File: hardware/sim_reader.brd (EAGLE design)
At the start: 29.2 x 20.3 mm, 15 parts, among them IC1 74AC04D, X1 3.57 MHz

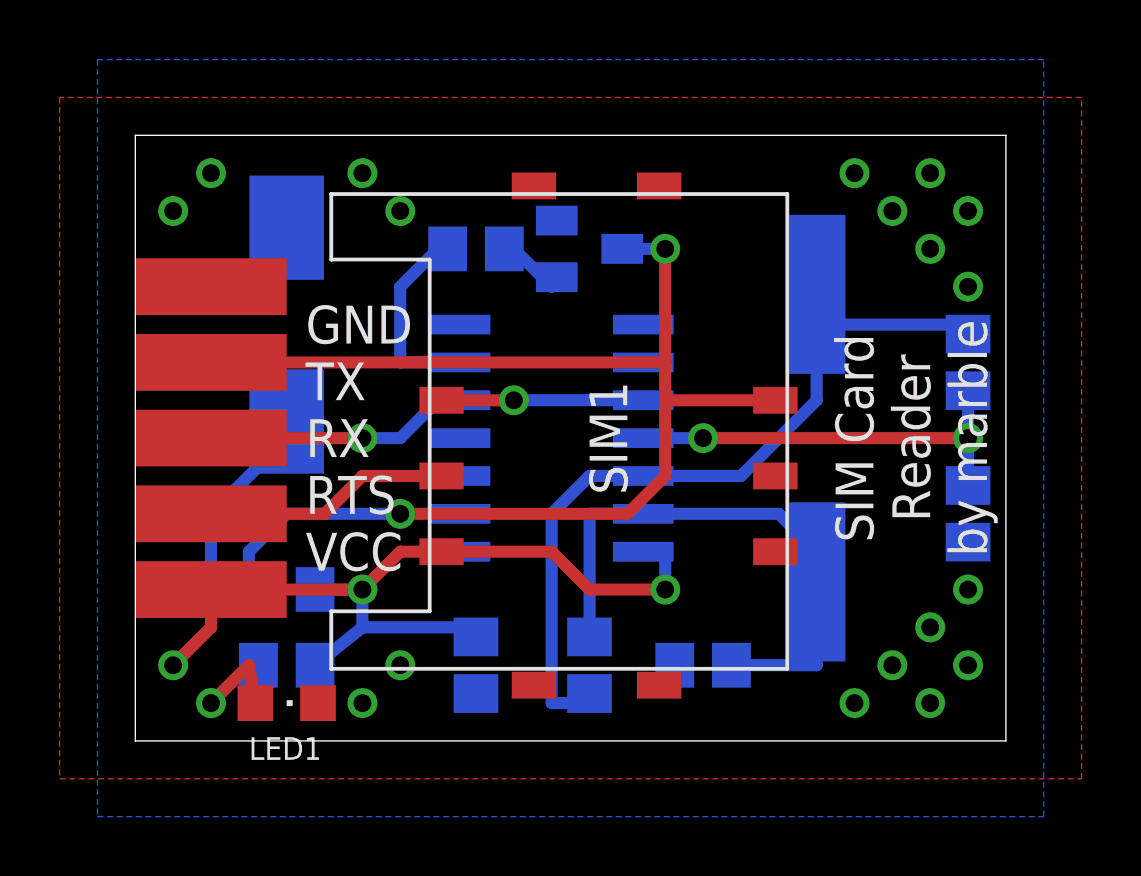
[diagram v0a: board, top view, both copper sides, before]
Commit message: redisgned. now compatible to most USB UART converters; very small
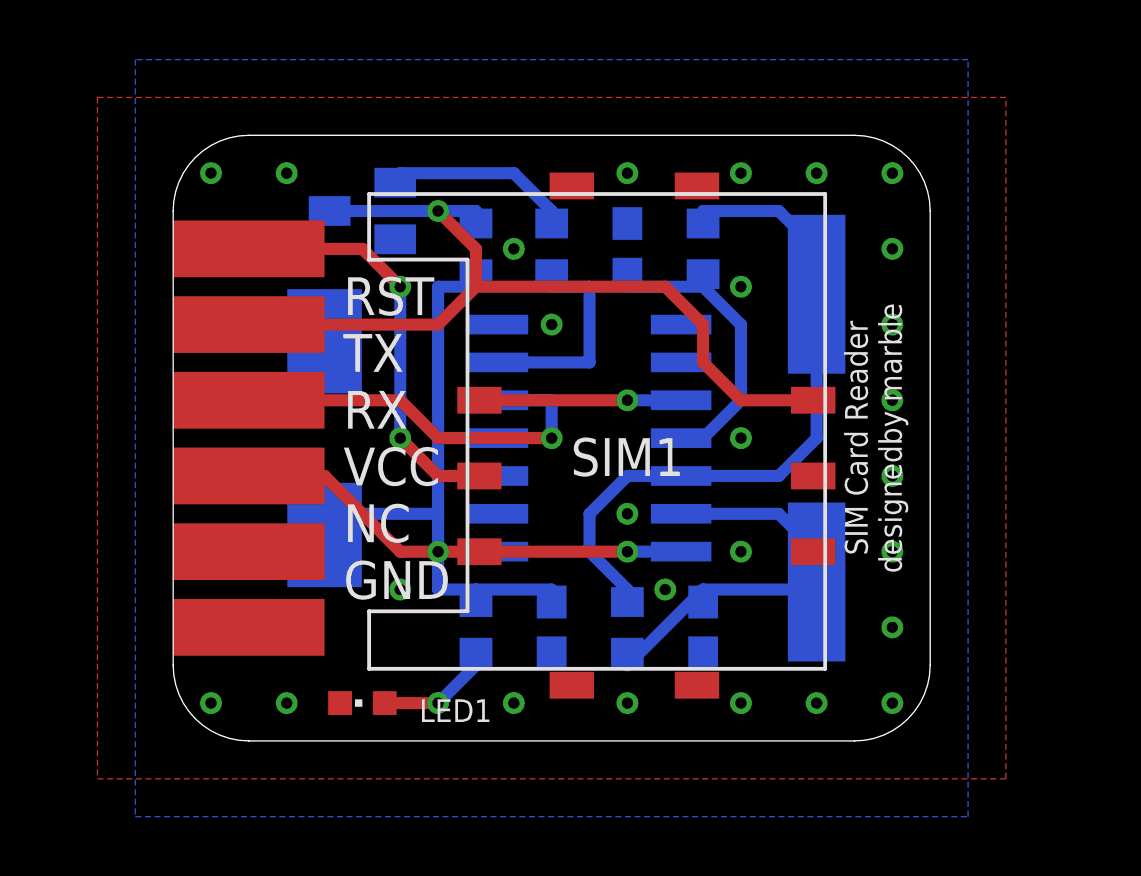
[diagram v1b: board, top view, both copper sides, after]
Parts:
- removed JP1: (no value), smd_pinhead:1X05
- removed R8: 1K, rcl:R0805
- added JP2: (no value), smd_pinhead:1X06
- added R5: 10K, rcl:R0603
- C1: value 1uF -> 20pF; device rcl:C0805 -> rcl:C0603
- C2: device rcl:C0805 -> rcl:C0603
- C3: value 20pF -> 1uF; device rcl:C0805 -> rcl:C0603
- LED1: device led:CHIPLED_0805 -> led:CHIPLED_0603
- Q1: value (none) -> BC808
- R1, R2, R4: device rcl:R0805 -> rcl:R0603
- R3: value 10K -> 1K; device rcl:R0805 -> rcl:R0603
- moved C2 14.5 mm to (15.2, 16.5), turned to 90 degrees
- moved R2 9.67 mm to (17.8, 16.5)
- moved C1 7.73 mm to (17.8, 3.81)
- moved Q1 7.73 mm to (6.35, 17.8), turned to 270 degrees
- moved R3 6.48 mm to (10.2, 3.81), turned to 270 degrees
- moved C3 5.24 mm to (12.7, 3.81), turned to 270 degrees
- moved C4 4.02 mm to (5.08, 10.2)
- moved LED1 2.54 mm to (6.35, 1.27), turned to 90 degrees
- moved R4 2.54 mm to (12.7, 16.5), turned to 270 degrees
- moved R1 1.80 mm to (15.2, 3.81), turned to 90 degrees
- moved IC1 1.27 mm to (14.0, 10.2)
- moved SIM1 1.27 mm to (15.2, 8.89)
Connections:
- net GND: now also IC1.9, JP2.6; no longer JP1.5
- net IO/RX: now also JP2.2, R5.1; no longer JP1.4, R3.1
- net N$1: now also C1.1; no longer C3.1
- net N$13: now also R3.2; no longer R8.2
- net RTS/RST: now also JP2.1; no longer JP1.2
- net TX: now also JP2.3; no longer JP1.3
- net VCC: now also C3.1, JP2.4, R3.1, R5.2; no longer C1.1, JP1.1, R3.2, R8.1
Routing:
- net IO/RX: track 44.6 -> 30.2 mm, vias 2 -> 1
- net TX: track 8.88 -> 14.5 mm
- net RTS/RST: track 8.26 -> 13.9 mm, vias 0 -> 2
- net N$1: track 18.9 -> 14.6 mm
- net N$2: track 27.4 -> 23.3 mm
- net N$6: track 2.51 -> 6.42 mm
- net N$3: track 14.1 -> 10.2 mm, vias 2 -> 0
- net VCC: track 40.1 -> 36.6 mm, vias 3 -> 2
- net N$13: track 5.20 -> 4.01 mm
- net N$4: track 6.66 -> 7.30 mm
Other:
- board size 29.2 x 20.3 mm -> 25.4 x 20.3 mm
- board text added: "RST TX RX VCC NC GND"
- board text added: "SIM Card Reader designedby marble"
- board text removed: "GND TX RX RTS VCC"
- board text removed: "SIM Card Reader by marble"
